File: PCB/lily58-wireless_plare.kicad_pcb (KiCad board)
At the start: 2 copper layers, 146.4 x 104.4 mm, 35 parts

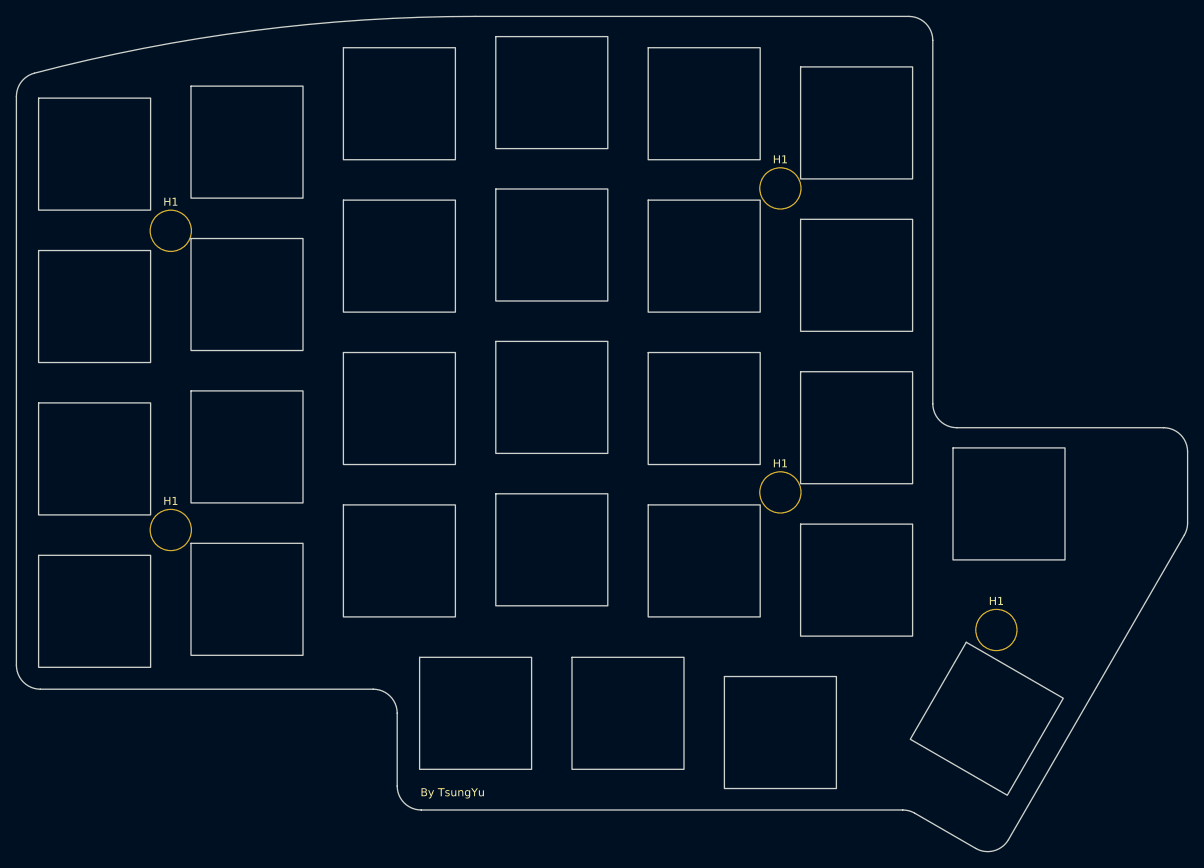
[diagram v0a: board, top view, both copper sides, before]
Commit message: FEAT: remove the wire part keep the wireless part
  - rename the project to "lily58-wireless"
  - add project symbol library
  - redesing the plate pcb
    - change the screw hole to 5mm
  - update the reset push buttom
  - update the README
    - keep the BOM up to date
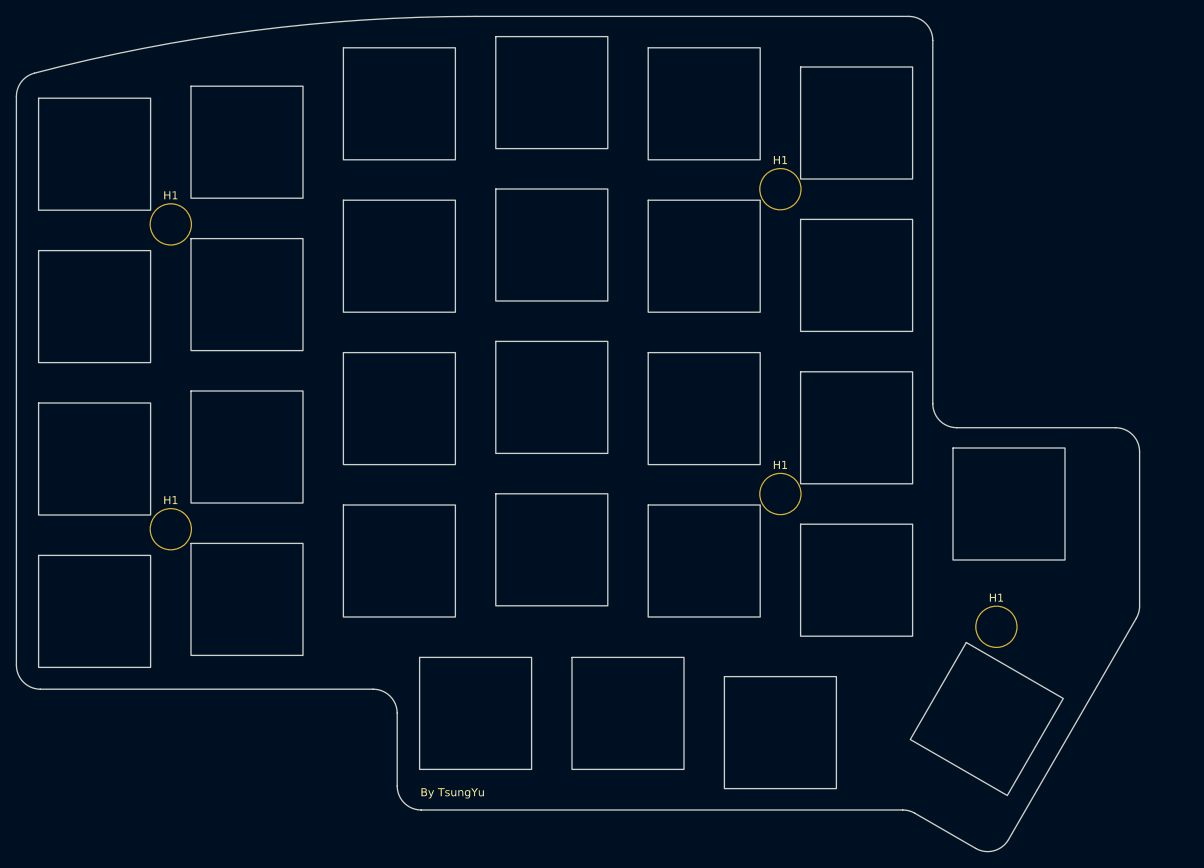
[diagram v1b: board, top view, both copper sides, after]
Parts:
- removed H2: MountingHole_Pad, tycharlie-lily58:MountingHole_3mm_Oval_Hole_ISO14580_Pad_TopBottom
- moved H1 0.80 mm to (81.0, 54.6)
- moved H1 0.40 mm to (184.2, 104.9)
- moved H1 0.20 mm to (157.2, 88.3)
- moved H1 0.10 mm to (157.2, 50.2)
- moved H1 0.10 mm to (81.0, 92.7)
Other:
- board size 146.4 x 104.4 mm -> 140.4 x 104.4 mm
